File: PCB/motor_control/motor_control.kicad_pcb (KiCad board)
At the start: 2 copper layers, 100 x 75 mm, 61 parts, among them J1 Screw, J11 MOT2, J12 AC in, J2 Screw, J5 Power, J6 Control Signals, J7 Sensor, J8 MOT1, J9 TRIAC_AUX1, K1 G2RL-1-E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

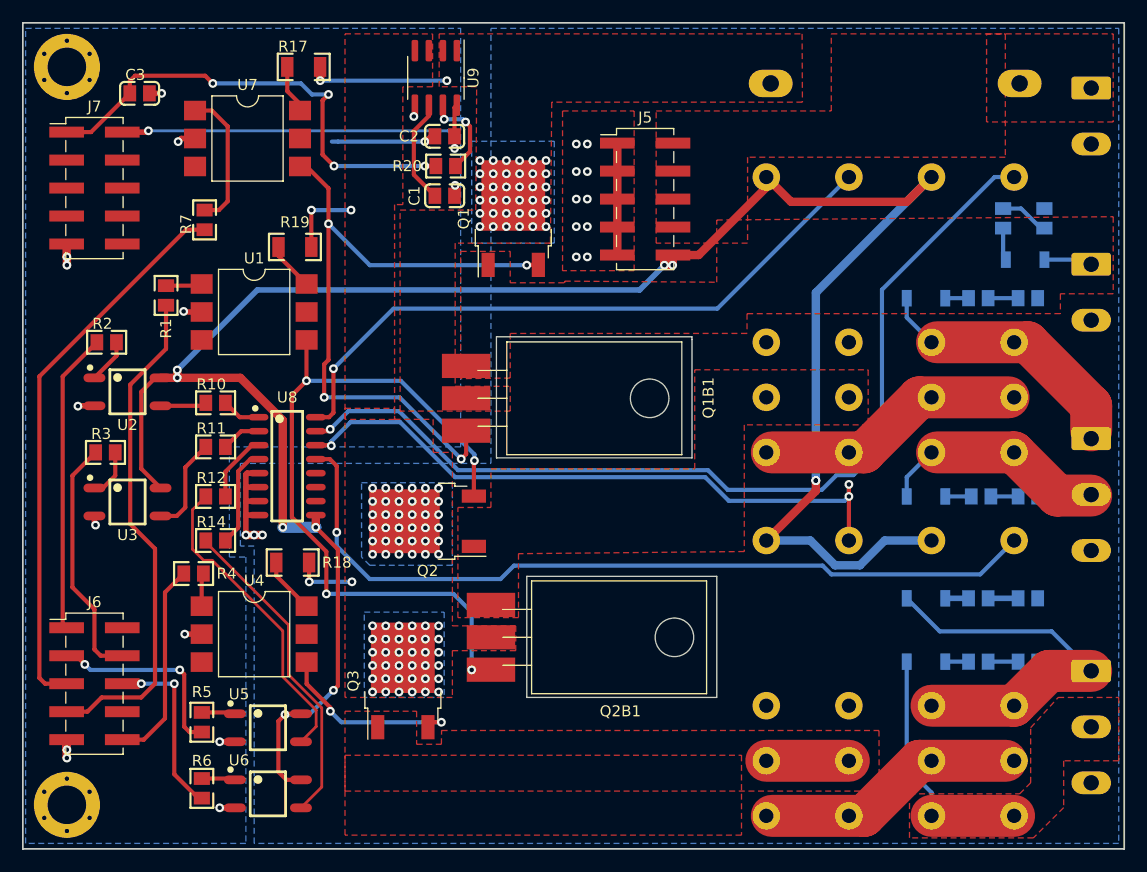
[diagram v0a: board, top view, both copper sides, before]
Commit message: Implemented the ESP-IDF version. First passed compilation
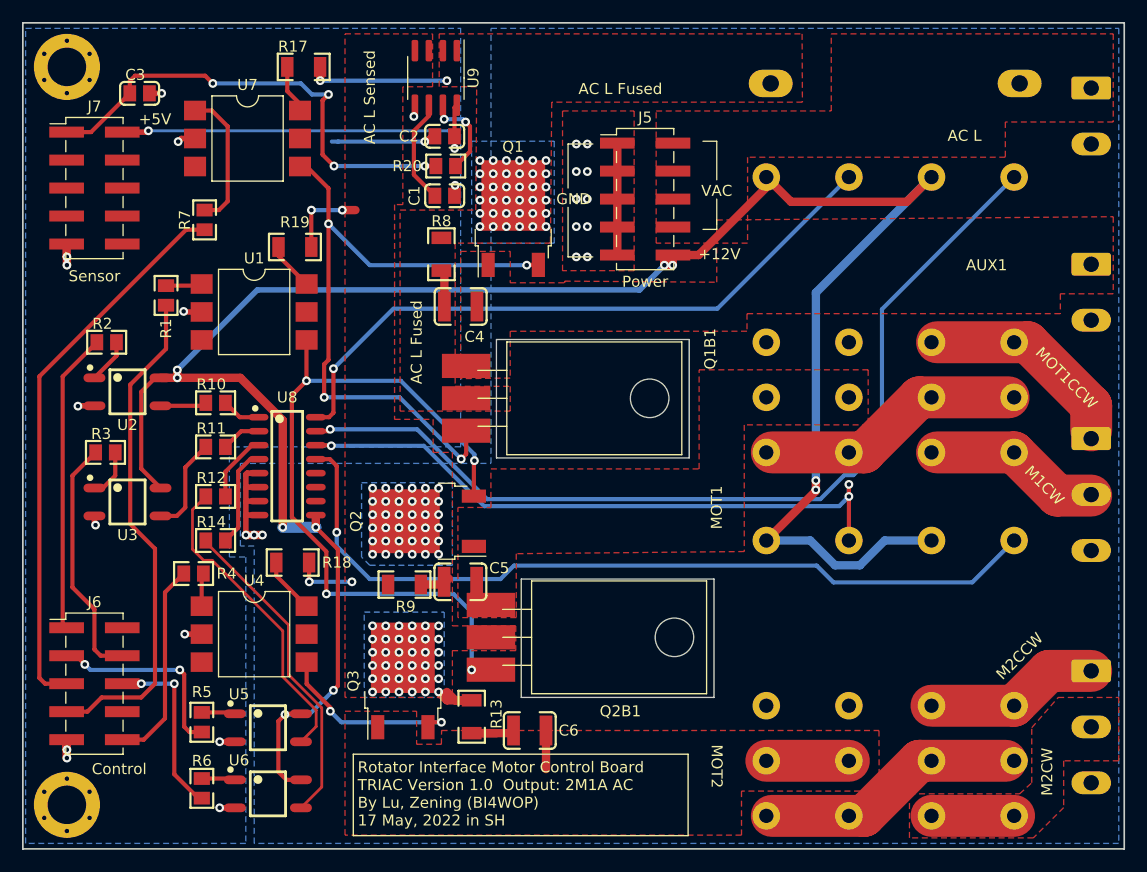
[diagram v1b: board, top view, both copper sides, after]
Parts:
- removed D1, D3, D5, D7, D9: 1N4148, MyPCBLib:LL-34
- removed D10, D2, D4, D6, D8: RED, MyPCBLib:0805_LED
- removed R15, R16: 4.7K, lc_lib:0805_R
- added C4: 103 100V, lc_lib:1210_C, F.Cu at (59.8, 45.8)
- added C5: 103 100V, lc_lib:1210_C, F.Cu at (59.7, 70.8)
- added C6: 103 100V, lc_lib:1210_C, F.Cu at (66.0, 84.2)
- R13, R8, R9: value 4.7K -> 100; footprint lc_lib:0805_R -> lc_lib:1206_R; moved to F.Cu
- moved R9 58.2 mm to (54.6, 71.0)
- moved R8 53.7 mm to (58.0, 41.0), turned to 270 degrees
- moved R13 46.3 mm to (60.8, 83.0), turned to 270 degrees
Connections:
- R13 pad 1: Net-(D5-Pad2) -> /AC_Mot
- R8 pad 1: Net-(D1-Pad2) -> /AC_in
- R9 pad 1: Net-(D3-Pad2) -> /AC_Mot
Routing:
- net /MOT2CCW: track 35.3 -> 15.8 mm
- net /MOT2CW: track 22.4 -> 7.50 mm
- net /AC_Mot: track 12.6 -> 18.9 mm
- net /MOT1CW: track 20.6 -> 15.6 mm
- net /MOT1CCW: track 23.6 -> 18.6 mm
- net Net-(D10-Pad1): track 4.49 -> 0.00 mm
- net /AUX1: track 4.42 -> 0.59 mm
- net /AC_MOT2: track 7.50 -> 11.0 mm
- net Net-(C6-Pad1): track 2.72 -> 6.16 mm
- net Net-(D9-Pad2): track 2.96 -> 0.00 mm
- net Net-(D8-Pad1): track 2.72 -> 0.00 mm
- net Net-(D1-Pad2): track 2.36 -> 0.00 mm
- net Net-(D7-Pad2): track 2.11 -> 0.00 mm
- net Net-(D5-Pad2): track 2.11 -> 0.00 mm
- net Net-(D3-Pad2): track 2.11 -> 0.00 mm
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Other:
- outline, holes or cut-outs redrawn
- board text added: "+12V"
- board text added: "+5V"
- board text added: "12Vac-30Vac"
- board text added: "15A"
- board text added: "AC"
- board text added: "AC L"
- board text added: "AC L Fused"
- board text added: "AC L Sensed"
- board text added: "AUX1"
- board text added: "CCW"
- board text added: "CW"
- board text added: "Control"
- board text added: "GND"
- board text added: "L"
- board text added: "M1CW"
- board text added: "M2CCW"
- board text added: "M2CW"
- board text added: "MOT1"
- board text added: "MOT1CCW"
- board text added: "MOT2"
- board text added: "N"
- board text added: "Power"
- board text added: "Rotator Interface Motor Control Board TRIAC Version 1.0 Output: 2M1A AC By Lu, Zening (BI4WOP) 17 May, 2022 in SH"
- board text added: "Sensor"
- board text added: "VAC"

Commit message: motor control board with SPWM support`
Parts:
- added D1: 1N4148, MyPCBLib:SOD-123, F.Cu at (106.2, 35.9)
- added D2: 1N4148, MyPCBLib:SOD-123, F.Cu at (91.2, 68.8)
- added D3: 1N4148, MyPCBLib:SOD-123, F.Cu at (106.3, 68.8)
- added D4: 1N4148, MyPCBLib:SOD-123, F.Cu at (91.3, 35.9)
- U9: value ACS712xLCTR-30A -> ACS712/CC6902
- turned J5 to 180 degrees
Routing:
- net GNDPWR: track 25.9 -> 15.7 mm, vias 13 -> 3
- net +12V: track 206.3 -> 199.0 mm, vias 10 -> 8
- net Net-(D1-Pad1): track 85.5 -> 88.6 mm
- net Net-(D2-Pad1): track 57.2 -> 60.3 mm
- net Net-(D4-Pad1): track 59.8 -> 62.8 mm
- net Net-(D3-Pad1): track 74.9 -> 77.8 mm
- removed copper zone on F.Cu, net GNDPWR
